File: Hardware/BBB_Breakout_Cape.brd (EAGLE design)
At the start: 1 part

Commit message: board ready for review
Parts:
- added C1: (no value), SparkFun-Capacitors:0603-CAP
- added FRAME1: FRAME-LETTER, SparkFun-Aesthetics:CREATIVE_COMMONS
- added JP1, JP2: (no value), SparkFun-Passives:SJ_2S-NO
- added LOGO2: OSHW-LOGOS, SparkFun-Aesthetics:OSHW-LOGO-S
- added LOGO3: SFE_LOGO_NAME_FLAME.1_INCH, SparkFun-Aesthetics:SFE_LOGO_NAME_FLAME_.1
- added R1, R2, R3, R4, R5: (no value), SparkFun-Resistors:0603
- added R6: (no value), SparkFun-Resistors:0603-RES
- added SJ1: (no value), SparkFun-Passives:SJ_3_PASTE1&2&3
- added SJ2: (no value), SparkFun-Passives:SJ_3_PASTE2&3
- added U$2, U$3, U$4, U$5: M23, SparkFun-Connectors:1X23
- added U1: EEPROM-I2CSMD, SparkFun-DigitalIC:SO08
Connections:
- new net 3.3V: C1.1, R1.2, R2.2, R3.2, SJ1.2, SJ2.1, U1.8
- new net A0: JP1.1, R3.1, U1.1
- new net A1: JP2.1, R2.1, U1.2
- new net GND: C1.2, JP1.2, JP2.2, SJ2.3, U$1.P8.1, U$1.P8.2, U$1.P9.1, U$1.P9.2, U$1.P9.43, U$1.P9.44, U$1.P9.45, U$1.P9.46, U$2.24, U$3.24, U$4.2, U$4.24, U$4.3, U$5.2, U$5.24, U$5.3, U1.4
- new net N$1: R6.1, U1.7
- new net N$10: R4.2, SJ1.3
- new net N$11: R5.2, SJ1.1
- new net N$12: U$1.P8.37, U$2.6
- new net N$13: U$1.P8.35, U$2.7
- new net N$14: U$1.P8.33, U$2.8
- new net N$15: U$1.P8.31, U$2.9
- new net N$16: U$1.P8.29, U$2.10
- new net N$17: U$1.P8.27, U$2.11
- new net N$18: U$1.P8.25, U$2.12
- new net N$19: U$1.P8.23, U$2.13
- new net N$2: U$1.P8.45, U$2.2
- new net N$20: U$1.P8.21, U$2.14
- new net N$21: U$1.P8.19, U$2.15
- new net N$22: U$1.P8.17, U$2.16
- new net N$23: U$1.P8.15, U$2.17
- new net N$24: U$1.P8.13, U$2.18
- new net N$25: U$1.P8.11, U$2.19
- new net N$26: U$1.P8.9, U$2.20
- new net N$27: U$1.P8.7, U$2.21
- new net N$28: U$1.P8.5, U$2.22
- new net N$29: U$1.P8.3, U$2.23
- new net N$3: R6.2, SJ2.2
- new net N$31: U$1.P8.46, U$3.2
- new net N$32: U$1.P8.44, U$3.3
- new net N$33: U$1.P8.42, U$3.4
- new net N$34: U$1.P8.40, U$3.5
- new net N$35: U$1.P8.38, U$3.6
- new net N$36: U$1.P8.36, U$3.7
- new net N$37: U$1.P8.34, U$3.8
- new net N$38: U$1.P8.32, U$3.9
- new net N$39: U$1.P8.30, U$3.10
- new net N$4: U$1.P8.43, U$2.3
- new net N$40: U$1.P8.28, U$3.11
- new net N$41: U$1.P8.26, U$3.12
- new net N$42: U$1.P8.24, U$3.13
- new net N$43: U$1.P8.22, U$3.14
- new net N$44: U$1.P8.20, U$3.15
- new net N$45: U$1.P8.18, U$3.16
- new net N$46: U$1.P8.16, U$3.17
- new net N$47: U$1.P8.14, U$3.18
- new net N$48: U$1.P8.12, U$3.19
- new net N$49: U$1.P8.10, U$3.20
- new net N$5: U$1.P8.41, U$2.4
- new net N$50: U$1.P8.8, U$3.21
- new net N$51: U$1.P8.6, U$3.22
- new net N$52: U$1.P8.4, U$3.23
- new net N$56: U$1.P9.42, U$5.4
- new net N$57: U$1.P9.40, U$5.5
- new net N$58: U$1.P9.38, U$5.6
- new net N$59: U$1.P9.36, U$5.7
- new net N$6: R1.1, U1.3
- new net N$60: U$1.P9.34, U$5.8
- new net N$61: U$1.P9.32, U$5.9
- new net N$62: U$1.P9.30, U$5.10
- new net N$63: U$1.P9.28, U$5.11
- new net N$64: U$1.P9.26, U$5.12
- new net N$65: U$1.P9.24, U$5.13
- new net N$66: U$1.P9.22, U$5.14
- new net N$68: U$1.P9.18, U$5.16
- new net N$69: U$1.P9.16, U$5.17
- new net N$70: U$1.P9.14, U$5.18
- new net N$71: U$1.P9.12, U$5.19
- new net N$72: U$1.P9.10, U$5.20
- new net N$73: U$1.P9.8, U$5.21
- new net N$74: U$1.P9.6, U$5.22
- new net N$75: U$1.P9.4, U$5.23
- new net N$79: U$1.P9.41, U$4.4
- new net N$80: U$1.P9.39, U$4.5
- new net N$81: U$1.P9.37, U$4.6
- new net N$82: U$1.P9.35, U$4.7
- new net N$83: U$1.P9.33, U$4.8
- new net N$84: U$1.P9.31, U$4.9
- new net N$85: U$1.P9.29, U$4.10
- new net N$86: U$1.P9.27, U$4.11
- new net N$87: U$1.P9.25, U$4.12
- new net N$88: U$1.P9.23, U$4.13
- new net N$89: U$1.P9.21, U$4.14
- new net N$9: U$1.P8.39, U$2.5
- new net N$91: U$1.P9.17, U$4.16
- new net N$92: U$1.P9.15, U$4.17
- new net N$93: U$1.P9.13, U$4.18
- new net N$94: U$1.P9.11, U$4.19
- new net N$95: U$1.P9.9, U$4.20
- new net N$96: U$1.P9.7, U$4.21
- new net N$97: U$1.P9.5, U$4.22
- new net N$98: U$1.P9.3, U$4.23
- new net SCL: R5.1, U$1.P9.19, U$4.15, U1.6
- new net SDA: R4.1, U$1.P9.20, U$5.15, U1.5
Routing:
- net SCL: track 0.00 -> 50.5 mm
- net SDA: track 0.00 -> 41.6 mm
- net 3.3V: track 0.00 -> 8.86 mm, vias 0 -> 2
- net A1: track 0.00 -> 7.19 mm
- net N$4: track 0.00 -> 6.77 mm
- net N$32: track 0.00 -> 6.77 mm
- net N$97: track 0.00 -> 6.77 mm
- net N$89: track 0.00 -> 6.77 mm
- net N$88: track 0.00 -> 6.77 mm
- net N$87: track 0.00 -> 6.77 mm
- net N$74: track 0.00 -> 6.77 mm
- net N$66: track 0.00 -> 6.77 mm
- net N$65: track 0.00 -> 6.77 mm
- net N$64: track 0.00 -> 6.77 mm
- net N$51: track 0.00 -> 6.77 mm
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- added copper zone on layer 1, net 3.3V
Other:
- board outline added: 86.4 x 54.6 mm
- board text added: "1"
- board text added: "2"
- board text added: "45"
- board text added: "46"
- board text added: "A0"
- board text added: "A1"
- board text added: "CAPE EEPROM"
- board text added: "Casey Kuhns"
- board text added: "I2C EN"
- board text added: "WP"

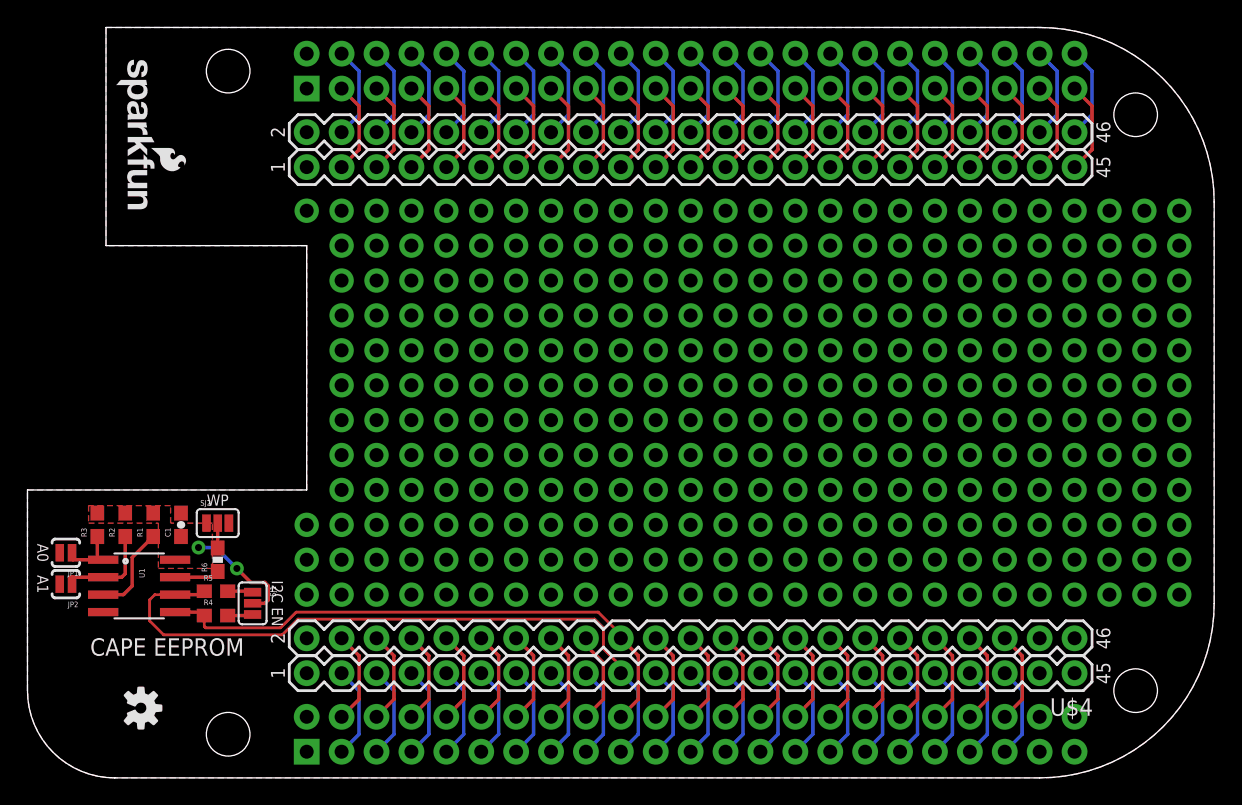
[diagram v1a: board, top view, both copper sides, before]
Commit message: Updated labels and corrected silk on bottom layer
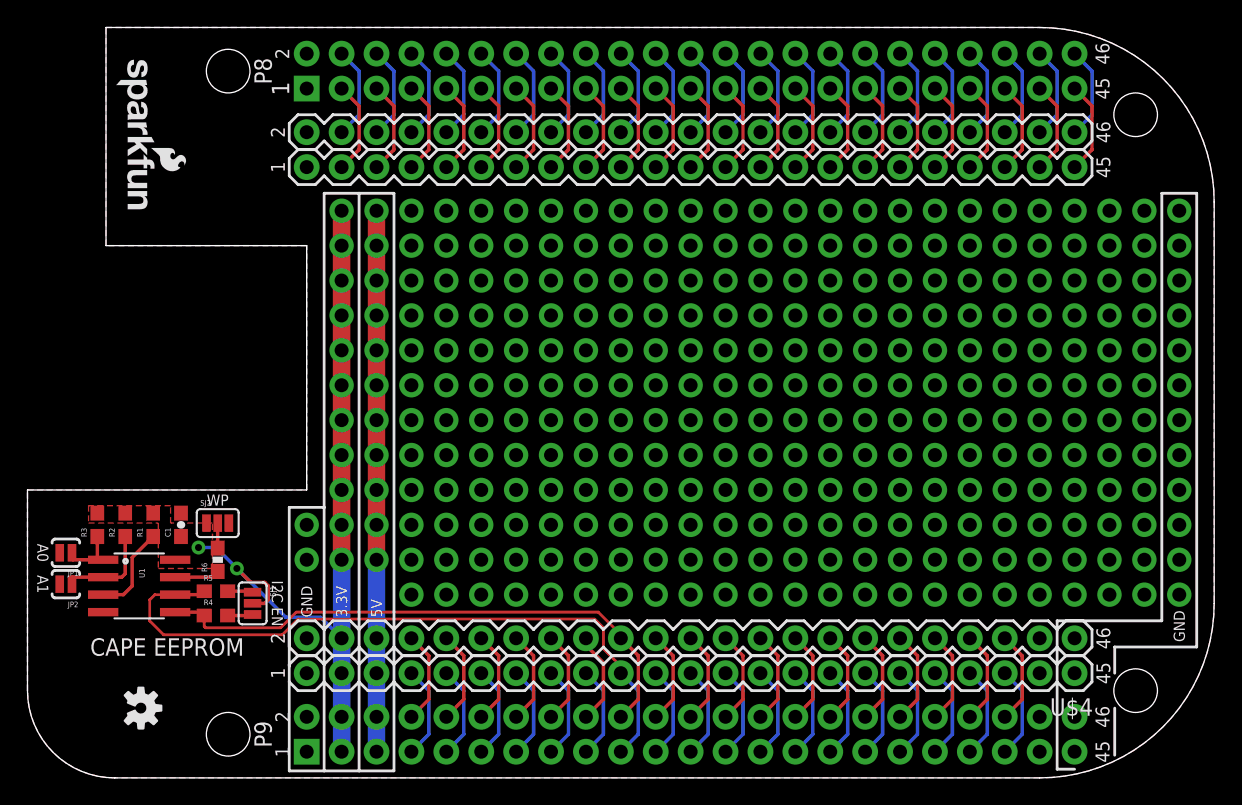
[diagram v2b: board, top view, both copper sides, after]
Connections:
- removed net N$74: U$1.P9.6, U$5.22
- removed net N$75: U$1.P9.4, U$5.23
- removed net N$97: U$1.P9.5, U$4.22
- removed net N$98: U$1.P9.3, U$4.23
- new net 5V: U$1.P9.5, U$1.P9.6, U$4.22, U$5.22
- net 3.3V: now also U$1.P9.3, U$1.P9.4, U$4.23, U$5.23
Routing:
- net 3.3V: track 8.86 -> 58.0 mm, vias 2 -> 13
- net 5V: track 0.00 -> 39.4 mm, vias 0 -> 11
- net N$97: track 6.77 -> 0.00 mm
- net N$74: track 6.77 -> 0.00 mm
- net N$98: track 6.77 -> 0.00 mm
- net N$75: track 6.77 -> 0.00 mm
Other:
- board text added: "3.3V"
- board text added: "5V"
- board text added: "GND"

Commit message: added labels and corrected WP jumper to eliminate possible short.
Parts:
- removed JP1, JP2: (no value), SparkFun-Passives:SJ_2S-NO
- removed SJ2: (no value), SparkFun-Passives:SJ_3_PASTE2&3
- added SJ3: A1, SparkFun-Passives:SJ_2S-NO
- added SJ4: A0, SparkFun-Passives:SJ_2S-NO
- added SJ5: WP, SparkFun-Passives:SJ_2S-NO
- C1: value (none) -> 0.1uF
- R1, R2, R3, R4, R5: value (none) -> 4.7k
- R6: value (none) -> 10k
- SJ1: value (none) -> I2C EN
- moved R6 0.90 mm to (13.7, 15.0), turned to 180 degrees
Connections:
- removed net N$3: R6.2, SJ2.2
- net 3.3V: now also SJ5.2; no longer SJ2.1
- net A0: now also SJ4.2; no longer JP1.1
- net A1: now also SJ3.2; no longer JP2.1
- net GND: now also R6.1, SJ3.1, SJ4.1; no longer JP1.2, JP2.2, SJ2.3
- net N$1: now also R6.2, SJ5.1; no longer R6.1
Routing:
- net N$1: track 3.49 -> 6.37 mm
- net N$3: track 1.82 -> 0.00 mm
- net 3.3V: track 58.0 -> 56.5 mm
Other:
- board text added: "v01"
